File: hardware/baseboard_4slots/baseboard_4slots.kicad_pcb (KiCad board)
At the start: 2 copper layers, 354 x 60 mm, 37 parts, among them J1 IO-Board_00, J2 IO-Board_01, J3 IO-Board_10, J4 IO-Board_11, J5 USB_B_Micro, J6 Conn_01x05: Adafruit 1833, J7 Screw_Terminal_01x04, J8 Conn_02x02_Odd_Even, J9 Conn_02x02_Odd_Even, U1 NRF24L01_Breakout, U2 Pico

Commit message: Hardware: Make the reference path to the library relative and save the files with the new kicad version
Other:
- net class Default removed

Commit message: More files cleaned up + Some work on baseboard
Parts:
- U2: footprint MCU_RPi:RPi_Pico_SMD_TH -> MCU_RaspberryPi_and_Boards:RPi_Pico_SMD_TH
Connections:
- J5 pad 2: (no net) -> unconnected-(J5-Pad2)
- J5 pad 3: (no net) -> unconnected-(J5-Pad3)
- J5 pad 4: (no net) -> unconnected-(J5-Pad4)
- J6 pad 2: (no net) -> unconnected-(J6-Pad2)
- J6 pad 3: (no net) -> unconnected-(J6-Pad3)
- J6 pad 4: (no net) -> unconnected-(J6-Pad4)
- U1 pad 8: (no net) -> unconnected-(U1-Pad8)
- U2 pad 30: Net-(U2-Pad30) -> unconnected-(U2-Pad30)
- U2 pad 31: Net-(U2-Pad31) -> unconnected-(U2-Pad31)
- U2 pad 32: Net-(U2-Pad32) -> unconnected-(U2-Pad32)
- U2 pad 35: Net-(U2-Pad35) -> unconnected-(U2-Pad35)
- U2 pad 37: Net-(U2-Pad37) -> unconnected-(U2-Pad37)
- U2 pad 40: Net-(U2-Pad40) -> unconnected-(U2-Pad40)
- U2 pad 41: Net-(U2-Pad41) -> unconnected-(U2-Pad41)
- U2 pad 42: Net-(U2-Pad42) -> unconnected-(U2-Pad42)
- U2 pad 43: Net-(U2-Pad43) -> unconnected-(U2-Pad43)
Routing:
- net GND: vias 238 -> 237
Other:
- board text added: "rp2040-dmxsun USB DMX baseboard 4 slots; Rev 0.2 https://www.openlighting.org"
- board text removed: "rp2040-dongle USB DMX baseboard 4 slots; Rev 0.1 https://www.openlighting.org"

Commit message: Some more work on the baseboard
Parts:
- added C14: 82µF, Capacitor_THT:CP_Radial_D6.3mm_P2.50mm, F.Cu at (162.8, 46.2)
- added C15: 82µF, Capacitor_THT:CP_Radial_D6.3mm_P2.50mm, F.Cu at (68.6, 83.3)
- added C16: 82µF, Capacitor_THT:CP_Radial_D6.3mm_P2.50mm, F.Cu at (174.7, 83.5)
- added C17: 82µF, Capacitor_THT:CP_Radial_D6.3mm_P2.50mm, F.Cu at (280.1, 83.5)
- added C18: 82µF, Capacitor_THT:CP_Radial_D6.3mm_P2.50mm, F.Cu at (369.9, 66.5)
- added C19: 82µF, Capacitor_THT:CP_Radial_D6.3mm_P2.50mm, F.Cu at (34.1, 71.1)
- added C20: 82µF, Capacitor_THT:CP_Radial_D6.3mm_P2.50mm, F.Cu at (275.3, 76.0)
- added C21: 100nF, Capacitor_SMD:C_0603_1608Metric, F.Cu at (33.2, 75.9)
- added C22: 100nF, Capacitor_SMD:C_0603_1608Metric, F.Cu at (271.1, 76.6)
- added C23: 1nF, Capacitor_SMD:C_0603_1608Metric, F.Cu at (33.2, 77.5)
- added C24: 1nF, Capacitor_SMD:C_0603_1608Metric, F.Cu at (269.7, 76.6)
- added C25: 82µF, Capacitor_THT:CP_Radial_D6.3mm_P2.50mm, F.Cu at (140.3, 69.5)
- added C26: 82µF, Capacitor_THT:CP_Radial_D6.3mm_P2.50mm, F.Cu at (343.0, 75.9)
- added C27: 100nF, Capacitor_SMD:C_0603_1608Metric, F.Cu at (139.5, 79.1)
- added C28: 100nF, Capacitor_SMD:C_0603_1608Metric, F.Cu at (351.6, 78.8)
- added C29: 1nF, Capacitor_SMD:C_0603_1608Metric, F.Cu at (139.6, 80.7)
- added C30: 1nF, Capacitor_SMD:C_0603_1608Metric, F.Cu at (351.6, 80.4)
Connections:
- net +3V3 renamed +3.3V
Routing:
- net +3.3V: track 529.4 -> 529.3 mm, vias 7 -> 6
- net GND: vias 237 -> 244
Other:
- board text added: "rp2040-dmxsun USB DMX baseboard 4 slots; Rev 0.2 https://github.com/OpenLightingProject/rp2040-dmxsun"
- board text removed: "rp2040-dmxsun USB DMX baseboard 4 slots; Rev 0.2 https://www.openlighting.org"

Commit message: Add I2C expansion connectors and a Grove connector for the status LEDs
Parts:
- added J10: Conn_01x04_Male, Connector:NS-Tech_Grove_1x04_P2mm_Vertical, F.Cu at (126.0, 71.5)
- added J11: Conn_01x04_Male, Connector:NS-Tech_Grove_1x04_P2mm_Vertical, F.Cu at (117.5, 71.5)
- added J12: Conn_01x04_Male, Connector:NS-Tech_Grove_1x04_P2mm_Vertical, F.Cu at (253.0, 54.5)
- added J13: Conn_01x04_Male, Connector_JST:JST_SH_BM04B-SRSS-TB_1x04-1MP_P1.00mm_Vertical, F.Cu at (98.0, 68.0)
- added J14: Conn_01x04_Male, Connector_JST:JST_SH_BM04B-SRSS-TB_1x04-1MP_P1.00mm_Vertical, F.Cu at (108.7, 68.2)
- moved C14 16.2 mm to (179.0, 45.0)
- moved C29 4.70 mm to (139.6, 76.0)
- moved C27 4.60 mm to (139.5, 74.5)
- moved C17 1.40 mm to (281.5, 83.5)
- moved C25 1.00 mm to (140.3, 68.5)
- moved C20 0.70 mm to (276.0, 76.0)
- moved C26 0.50 mm to (342.5, 75.9)
- moved C22 0.40 mm to (271.5, 76.6)
- moved C28 0.20 mm to (351.8, 78.8)
- moved C30 0.17 mm to (351.8, 80.4)
- moved C21 0.07 mm to (33.3, 75.9)
- moved C23 0.07 mm to (33.3, 77.5)
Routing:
- net +3.3V: track 529.3 -> 571.8 mm, vias 6 -> 9
- net /SCL: track 429.9 -> 467.8 mm
- net /SDA: track 405.4 -> 440.8 mm, vias 5 -> 6
- net /STATUS_LEDS: track 30.1 -> 45.6 mm
- net VDD: track 553.1 -> 565.3 mm
- net GND: vias 244 -> 262
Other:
- board text added: "Grove I2C 3.3V"
- board text added: "Grove RGB LED WS2813 5V DC"
- board text added: "Qwiic / Stemma QT I2C 3.3V"

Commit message: Hardware: move some capacitors around to fix the DRC errors
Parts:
- moved C28 12.6 mm to (339.4, 76.6), turned to -90 degrees
- moved C30 10.1 mm to (342.4, 76.6), turned to -90 degrees
- moved C26 8.50 mm to (334.0, 75.9)
- moved C23 5.81 mm to (34.4, 83.2)
- moved C20 2.20 mm to (278.2, 76.0)
- moved C17 2.10 mm to (283.6, 83.5)
- moved C22 2.10 mm to (273.6, 76.6)
- moved C24 2.10 mm to (271.8, 76.6)
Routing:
- net GND: vias 262 -> 260
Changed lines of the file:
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@@
   )
   (footprint "Capacitor_SMD:C_0603_1608Metric" (layer "F.Cu")
-    (at 351.775 80.4 180)
+    (at 342.4 76.6 -90)
     (descr "Capacitor SMD 0603 (1608 Metric), square (rectangular) end terminal, IPC_7351 nominal, (Body size source: IPC-SM-782 page 76, https://www.pcb-3d.com/wordpress/wp-content/uploads/ipc-sm-782a_amendment_1_and_2.pdf), generated with kicad-footprint-generator")
     (tags "capacitor")
@@
     (property "Sheetname" "")
     (attr smd)
-    (fp_text reference "C30" (at 1.8 -2.4 90) (layer "F.SilkS")
+    (fp_text reference "C30" (at 2.4 -0.2) (layer "F.SilkS")
       (effects (font (size 1 1) (thickness 0.15)))
     )
-    (fp_text value "1nF" (at 0 1.43) (layer "F.Fab")
+    (fp_text value "1nF" (at 0 1.43 -270) (layer "F.Fab")
       (effects (font (size 1 1) (thickness 0.15)))
     )
-    (fp_text user "${REFERENCE}" (at 0 0) (layer "F.Fab")
+    (fp_text user "${REFERENCE}" (at 0 0 -270) (layer "F.Fab")
       (effects (font (size 0.4 0.4) (thickness 0.06)))
     )
@@
     (fp_line (start -0.8 0.4) (end -0.8 -0.4) (layer "F.Fab") (width 0.1))
     (fp_line (start 0.8 -0.4) (end 0.8 0.4) (layer "F.Fab") (width 0.1))
-    (pad "1" smd roundrect (at -0.775 0 180) (size 0.9 0.95) (layers "F.Cu" "F.Paste" "F.Mask") (roundrect_rratio 0.25)
+    (pad "1" smd roundrect (at -0.775 0 270) (size 0.9 0.95) (layers "F.Cu" "F.Paste" "F.Mask") (roundrect_rratio 0.25)
       (net 3 "+3.3V") (pintype "passive"))
-    (pad "2" smd roundrect (at 0.775 0 180) (size 0.9 0.95) (layers "F.Cu" "F.Paste" "F.Mask") (roundrect_rratio 0.25)
+    (pad "2" smd roundrect (at 0.775 0 270) (size 0.9 0.95) (layers "F.Cu" "F.Paste" "F.Mask") (roundrect_rratio 0.25)
       (net 1 "GND") (pintype "passive"))
     (model "${KICAD6_3DMODEL_DIR}/Capacitor_SMD.3dshapes/C_0603_1608Metric.wrl"
@@
   )
   (footprint "Capacitor_THT:CP_Radial_D6.3mm_P2.50mm" (layer "F.Cu")
-    (at 281.5 83.482379 90)
+    (at 283.6 83.482379 90)
     (descr "CP, Radial series, Radial, pin pitch=2.50mm, , diameter=6.3mm, Electrolytic Capacitor")
     (tags "CP Radial series Radial pin pitch 2.50mm  diameter 6.3mm Electrolytic Capacitor")
@@
   )
   (footprint "Capacitor_THT:CP_Radial_D6.3mm_P2.50mm" (layer "F.Cu")
-    (at 276 76 -90)
+    (at 278.2 76 -90)
     (descr "CP, Radial series, Radial, pin pitch=2.50mm, , diameter=6.3mm, Electrolytic Capacitor")
     (tags "CP Radial series Radial pin pitch 2.50mm  diameter 6.3mm Electrolytic Capacitor")
@@
   )
   (footprint "Capacitor_SMD:C_0603_1608Metric" (layer "F.Cu")
-    (at 269.7 76.625 -90)
+    (at 271.8 76.625 -90)
     (descr "Capacitor SMD 0603 (1608 Metric), square (rectangular) end terminal, IPC_7351 nominal, (Body size source: IPC-SM-782 page 76, https://www.pcb-3d.com/wordpress/wp-content/uploads/ipc-sm-782a_amendment_1_and_2.pdf), generated with kicad-footprint-generator")
     (tags "capacitor")
@@
   )
   (footprint "Capacitor_THT:CP_Radial_D6.3mm_P2.50mm" (layer "F.Cu")
-    (at 342.5 75.917621 -90)
+    (at 334 75.917621 -90)
     (descr "CP, Radial series, Radial, pin pitch=2.50mm, , diameter=6.3mm, Electrolytic Capacitor")
     (tags "CP Radial series Radial pin pitch 2.50mm  diameter 6.3mm Electrolytic Capacitor")
@@
   )
   (footprint "Capacitor_SMD:C_0603_1608Metric" (layer "F.Cu")
-    (at 33.275 77.5 180)
+    (at 34.425 83.2 180)
     (descr "Capacitor SMD 0603 (1608 Metric), square (rectangular) end terminal, IPC_7351 nominal, (Body size source: IPC-SM-782 page 76, https://www.pcb-3d.com/wordpress/wp-content/uploads/ipc-sm-782a_amendment_1_and_2.pdf), generated with kicad-footprint-generator")
     (tags "capacitor")
@@
     (property "Sheetname" "")
     (attr smd)
-    (fp_text reference "C23" (at 0 -1.43) (layer "F.SilkS")
+    (fp_text reference "C23" (at 3.025 -1) (layer "F.SilkS")
       (effects (font (size 1 1) (thickness 0.15)))
     )
@@
   )
   (footprint "Capacitor_SMD:C_0603_1608Metric" (layer "F.Cu")
-    (at 351.775 78.8 180)
+    (at 339.4 76.625 -90)
     (descr "Capacitor SMD 0603 (1608 Metric), square (rectangular) end terminal, IPC_7351 nominal, (Body size source: IPC-SM-782 page 76, https://www.pcb-3d.com/wordpress/wp-content/uploads/ipc-sm-782a_amendment_1_and_2.pdf), generated with kicad-footprint-generator")
     (tags "capacitor")
@@
     (property "Sheetname" "")
     (attr smd)
-    (fp_text reference "C28" (at -0.325 2) (layer "F.SilkS")
+    (fp_text reference "C28" (at 2.375 0 -180) (layer "F.SilkS")
       (effects (font (size 1 1) (thickness 0.15)))
     )
-    (fp_text value "100nF" (at 0 1.43) (layer "F.Fab")
+    (fp_text value "100nF" (at 0 1.43 -270) (layer "F.Fab")
       (effects (font (size 1 1) (thickness 0.15)))
     )
-    (fp_text user "${REFERENCE}" (at 0 0) (layer "F.Fab")
+    (fp_text user "${REFERENCE}" (at 0 0 -270) (layer "F.Fab")
       (effects (font (size 0.4 0.4) (thickness 0.06)))
     )
@@
     (fp_line (start -0.8 0.4) (end -0.8 -0.4) (layer "F.Fab") (width 0.1))
     (fp_line (start -0.8 -0.4) (end 0.8 -0.4) (layer "F.Fab") (width 0.1))
-    (pad "1" smd roundrect (at -0.775 0 180) (size 0.9 0.95) (layers "F.Cu" "F.Paste" "F.Mask") (roundrect_rratio 0.25)
+    (pad "1" smd roundrect (at -0.775 0 270) (size 0.9 0.95) (layers "F.Cu" "F.Paste" "F.Mask") (roundrect_rratio 0.25)
       (net 3 "+3.3V") (pintype "passive"))
-    (pad "2" smd roundrect (at 0.775 0 180) (size 0.9 0.95) (layers "F.Cu" "F.Paste" "F.Mask") (roundrect_rratio 0.25)
+    (pad "2" smd roundrect (at 0.775 0 270) (size 0.9 0.95) (layers "F.Cu" "F.Paste" "F.Mask") (roundrect_rratio 0.25)
       (net 1 "GND") (pintype "passive"))
     (model "${KICAD6_3DMODEL_DIR}/Capacitor_SMD.3dshapes/C_0603_1608Metric.wrl"
@@
   )
   (footprint "Capacitor_SMD:C_0603_1608Metric" (layer "F.Cu")
-    (at 271.5 76.6 -90)
+    (at 273.6 76.6 -90)
     (descr "Capacitor SMD 0603 (1608 Metric), square (rectangular) end terminal, IPC_7351 nominal, (Body size source: IPC-SM-782 page 76, https://www.pcb-3d.com/wordpress/wp-content/uploads/ipc-sm-782a_amendment_1_and_2.pdf), generated with kicad-footprint-generator")
     (tags "capacitor")
@@
   (via (at 229.978 76.562) (size 0.8) (drill 0.4) (layers "F.Cu" "B.Cu") (net 1))
   (via (at 272.396 79.991) (size 0.8) (drill 0.4) (layers "F.Cu" "B.Cu") (net 1))
-  (via (at 281 77.5) (size 0.8) (drill 0.4) (layers "F.Cu" "B.Cu") (net 1))
   (via (at 345.5 81) (size 0.8) (drill 0.4) (layers "F.Cu" "B.Cu") (net 1))
   (via (at 338 78) (size 0.8) (drill 0.4) (layers "F.Cu" "B.Cu") (net 1))
@@
   (via (at 202 29) (size 0.8) (drill 0.4) (layers "F.Cu" "B.Cu") (net 1))
   (via (at 238.614 26.778) (size 0.8) (drill 0.4) (layers "F.Cu" "B.Cu") (net 1))
-  (via (at 28.048 76.308) (size 0.8) (drill 0.4) (layers "F.Cu" "B.Cu") (net 1))
+  (via (at 28.2 76) (size 0.8) (drill 0.4) (layers "F.Cu" "B.Cu") (net 1))
   (via (at 247.377 34.398) (size 0.8) (drill 0.4) (layers "F.Cu" "B.Cu") (net 1))
   (via (at 217.278 66.402) (size 0.8) (drill 0.4) (layers "F.Cu" "B.Cu") (net 1))
@@
   (via (at 199.498 41.764) (size 0.8) (drill 0.4) (layers "F.Cu" "B.Cu") (net 1))
   (via (at 347.834 71.228) (size 0.8) (drill 0.4) (layers "F.Cu" "B.Cu") (net 1))
-  (via (at 29.572 76.308) (size 0.8) (drill 0.4) (layers "F.Cu" "B.Cu") (net 1))
+  (via (at 29.572 76) (size 0.8) (drill 0.4) (layers "F.Cu" "B.Cu") (net 1))
   (via (at 234.804 53.194) (size 0.8) (drill 0.4) (layers "F.Cu" "B.Cu") (net 1))
   (via (at 172 43.5) (size 0.8) (drill 0.4) (layers "F.Cu" "B.Cu") (net 1))
@@
   (via (at 260.458 72.498) (size 0.8) (drill 0.4) (layers "F.Cu" "B.Cu") (net 1))
   (via (at 34.8 67) (size 0.8) (drill 0.4) (layers "F.Cu" "B.Cu") (net 1))
-  (via (at 31.096 76.308) (size 0.8) (drill 0.4) (layers "F.Cu" "B.Cu") (net 1))
+  (via (at 31.096 76) (size 0.8) (drill 0.4) (layers "F.Cu" "B.Cu") (net 1))
   (via (at 247.5 45) (size 0.8) (drill 0.4) (layers "F.Cu" "B.Cu") (net 1))
   (via (at 355.962 75.673) (size 0.8) (drill 0.4) (layers "F.Cu" "B.Cu") (net 1))
@@
   (via (at 230.74 26.651) (size 0.8) (drill 0.4) (layers "F.Cu" "B.Cu") (net 1))
   (via (at 242.805 28.556) (size 0.8) (drill 0.4) (layers "F.Cu" "B.Cu") (net 1))
-  (via (at 358.756 82.023) (size 0.8) (drill 0.4) (layers "F.Cu" "B.Cu") (net 1))
   (via (at 263.379 75.927) (size 0.8) (drill 0.4) (layers "F.Cu" "B.Cu") (net 1))
   (via (at 234.804 40.494) (size 0.8) (drill 0.4) (layers "F.Cu" "B.Cu") (net 1))

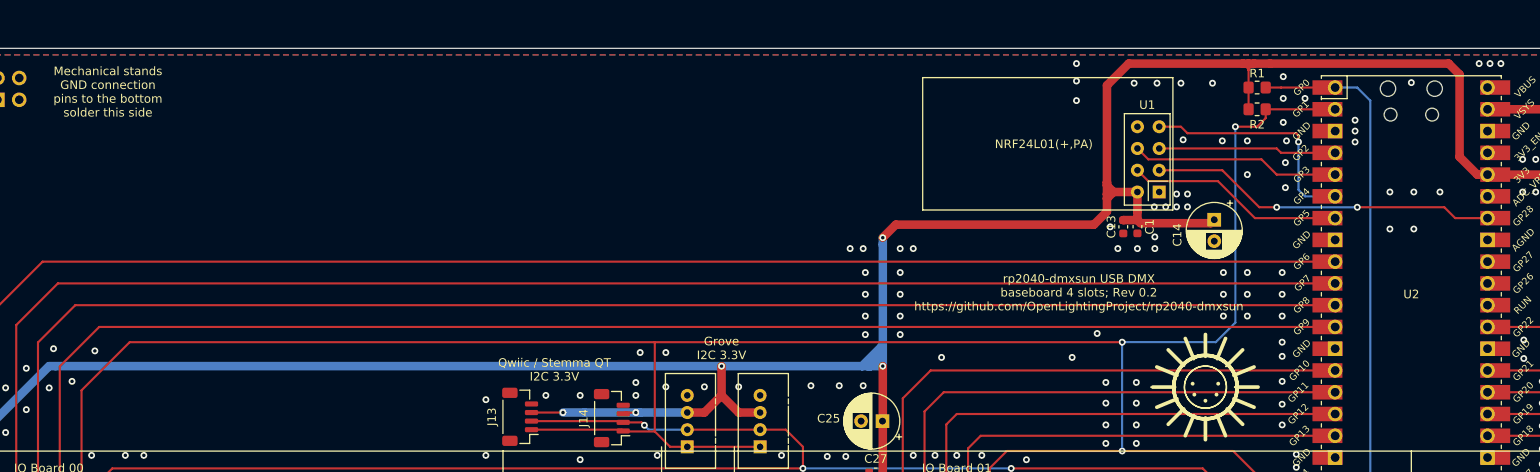
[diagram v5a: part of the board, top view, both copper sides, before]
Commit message: Baseboard: Add W5500 Mini (WIZ850io) module. Needs verification
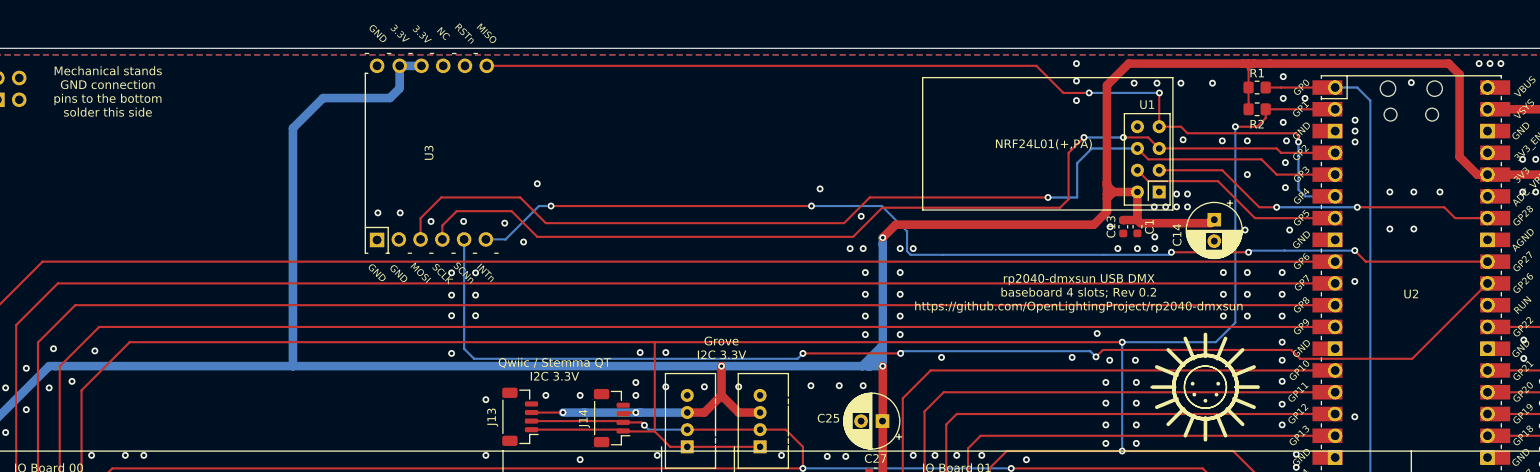
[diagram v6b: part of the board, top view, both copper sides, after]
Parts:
- added U3: W5500_Mini, W5500_Mini:W5500_Mini, F.Cu at (87.4, 37.2)
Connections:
- U2 pad 31: unconnected-(U2-Pad31) -> /SPI_CS1
- U2 pad 32: unconnected-(U2-Pad32) -> /WIZ_INT
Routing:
- net /SPI_CS1: track 0.00 -> 137.7 mm, vias 0 -> 3
- net /WIZ_INT: track 0.00 -> 123.0 mm, vias 0 -> 5
- net /SPI_CLK: track 20.7 -> 116.5 mm, vias 0 -> 2
- net /SPI_MOSI: track 24.3 -> 118.7 mm, vias 0 -> 1
- net /SPI_MISO: track 27.6 -> 111.4 mm, vias 1 -> 3
- net +3.3V: track 571.8 -> 619.2 mm
- net GND: vias 260 -> 282

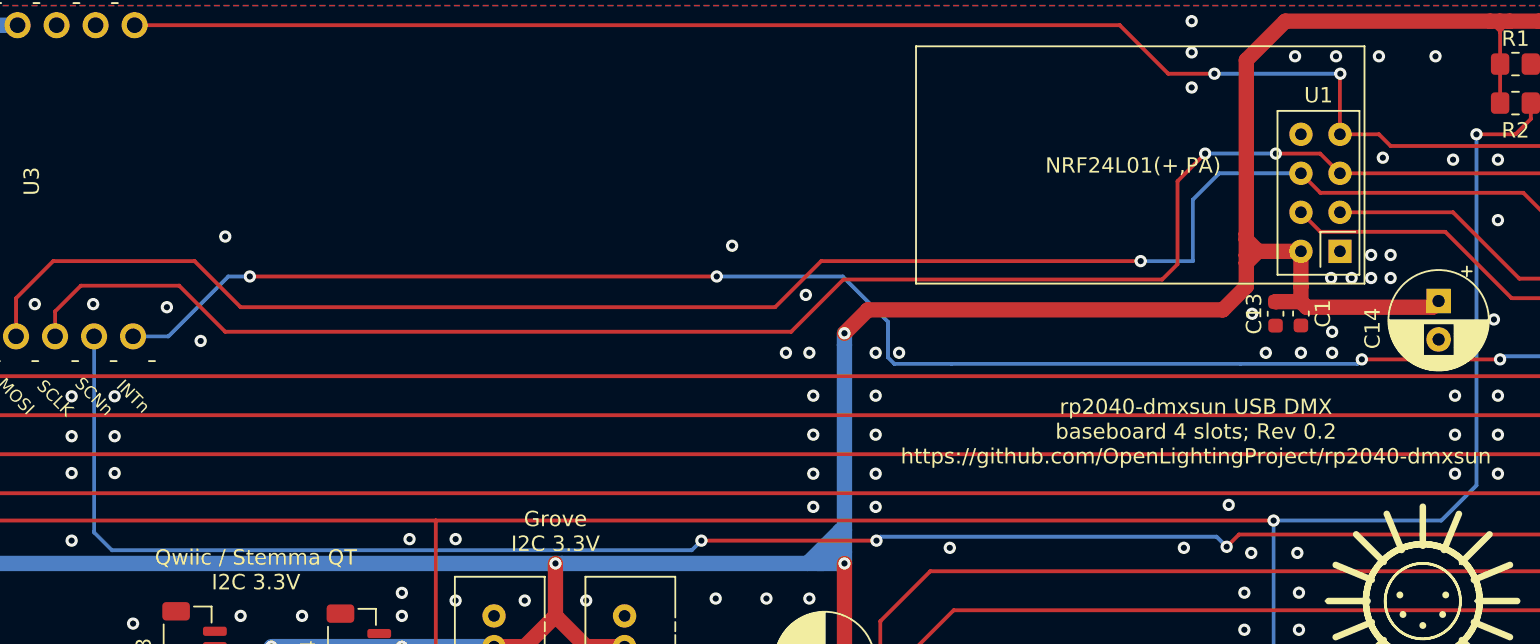
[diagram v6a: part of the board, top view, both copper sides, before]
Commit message: Connect the nRF24 to the now shared IRQ line and supress some ERC errors
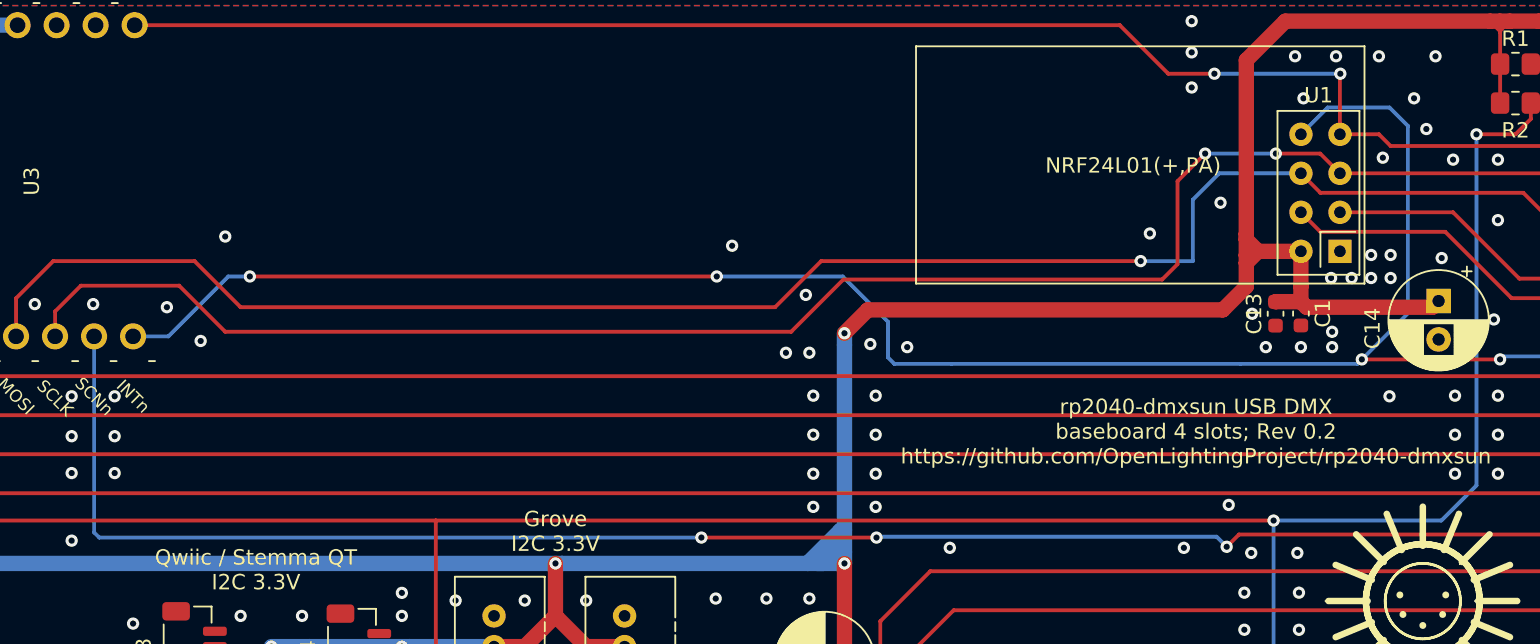
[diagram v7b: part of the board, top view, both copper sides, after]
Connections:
- U1 pad 8: unconnected-(U1-Pad8) -> /WIZ_NRF_INT
- U2 pad 32: /WIZ_INT -> /WIZ_NRF_INT
- U3 pad 6: /WIZ_INT -> /WIZ_NRF_INT
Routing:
- net /WIZ_NRF_INT: track 0.00 -> 147.6 mm, vias 0 -> 5
- net /WIZ_INT: track 123.0 -> 0.00 mm, vias 5 -> 0
- net /SPI_CS1: track 137.7 -> 136.9 mm
- net GND: vias 282 -> 287

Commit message: Update W5500_Mini footprint and minor fixes on the baseboard
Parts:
- added J15: Conn_02x02_Odd_Even, Connector_PinSocket_2.54mm:PinSocket_2x02_P2.54mm_Vertical, F.Cu at (149.8, 35.3)
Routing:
- net /SPI_MOSI: track 118.7 -> 120.7 mm
- net /WIZ_NRF_INT: track 147.6 -> 149.5 mm, vias 5 -> 2
- net /SPI_CLK: track 116.5 -> 117.8 mm
- net /SCL: track 467.8 -> 469.1 mm
- net /SPI_CS1: track 136.9 -> 136.3 mm, vias 3 -> 1
- net /IO2_GP1: track 65.4 -> 64.8 mm
- net GND: vias 287 -> 312
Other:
- board text added: "Raspberry Pi Pico or Pico-W"
- board text added: "WizNet W5500 Mini WIZ850io"
- board text added: "rp2040-dmxsun USB DMX baseboard 4 slots; Rev 0.5 https://github.com/OpenLightingProject/rp2040-dmxsun"
- board text removed: "rp2040-dmxsun USB DMX baseboard 4 slots; Rev 0.2 https://github.com/OpenLightingProject/rp2040-dmxsun"
